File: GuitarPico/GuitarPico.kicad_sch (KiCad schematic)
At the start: 132 parts, among them J1 INPUT, J2 INPUT, J3 OUTPUT, J4 OUTPUT, J5 Barrel_Jack_Switch, J6 VGA, J8 INPUT, J9 INPUT, Q1 2N3904, Q2 2N3904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

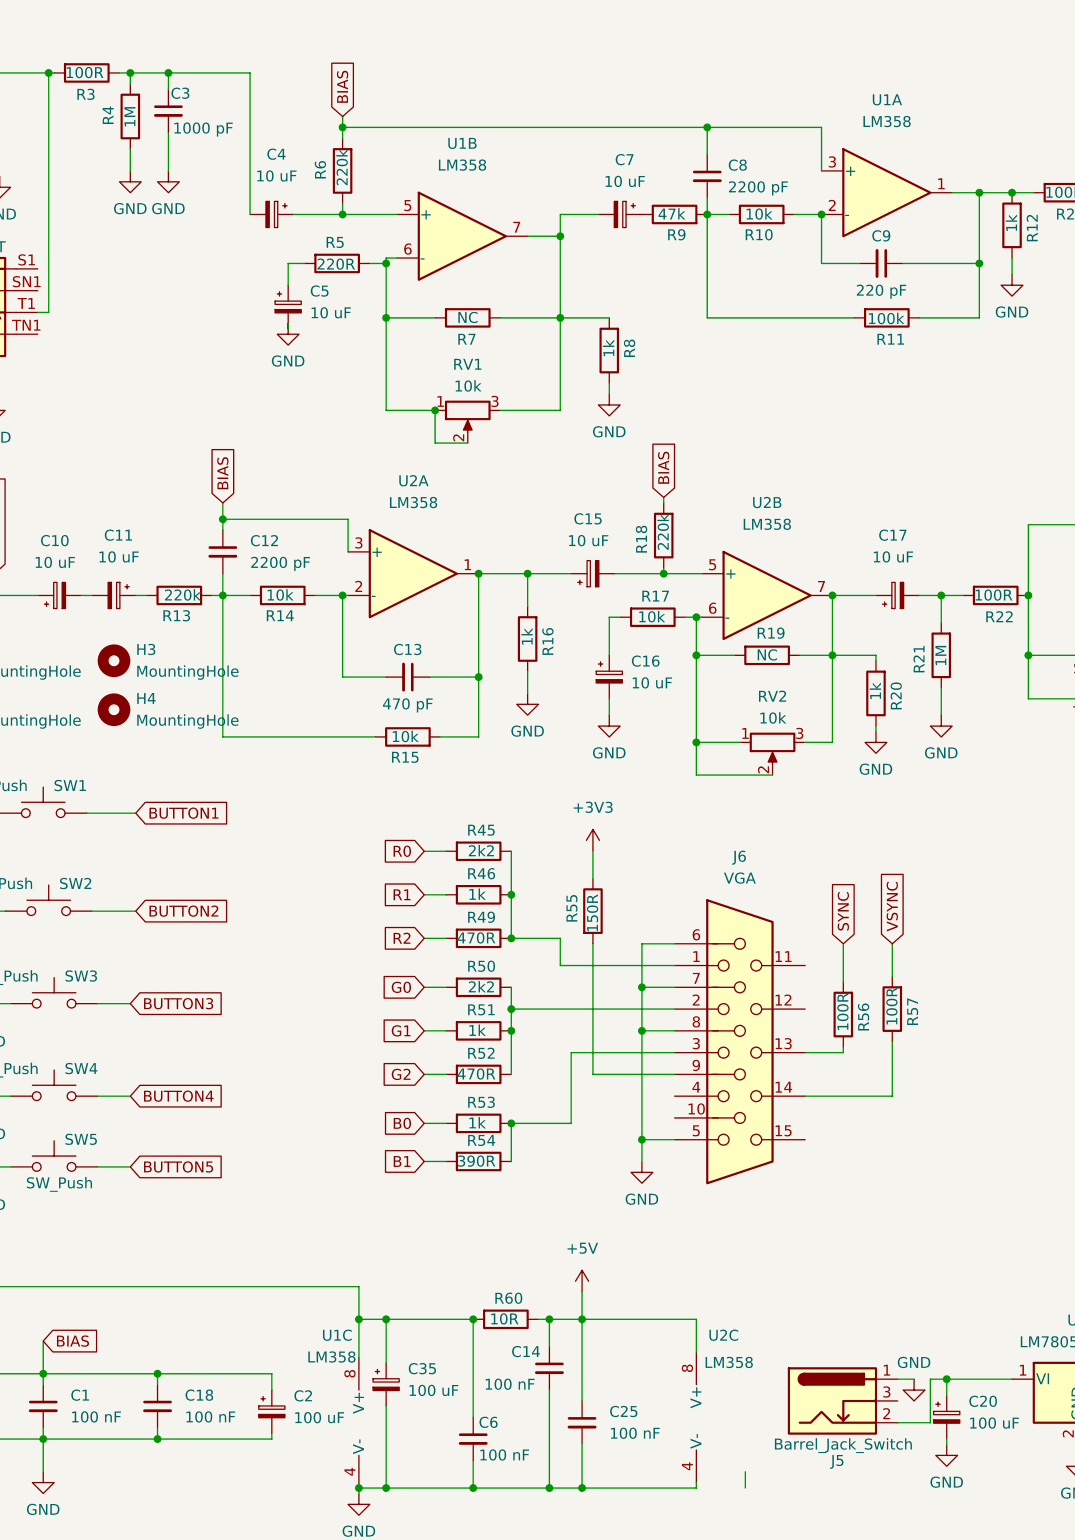
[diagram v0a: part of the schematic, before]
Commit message: Added STL file for pedal enclosure
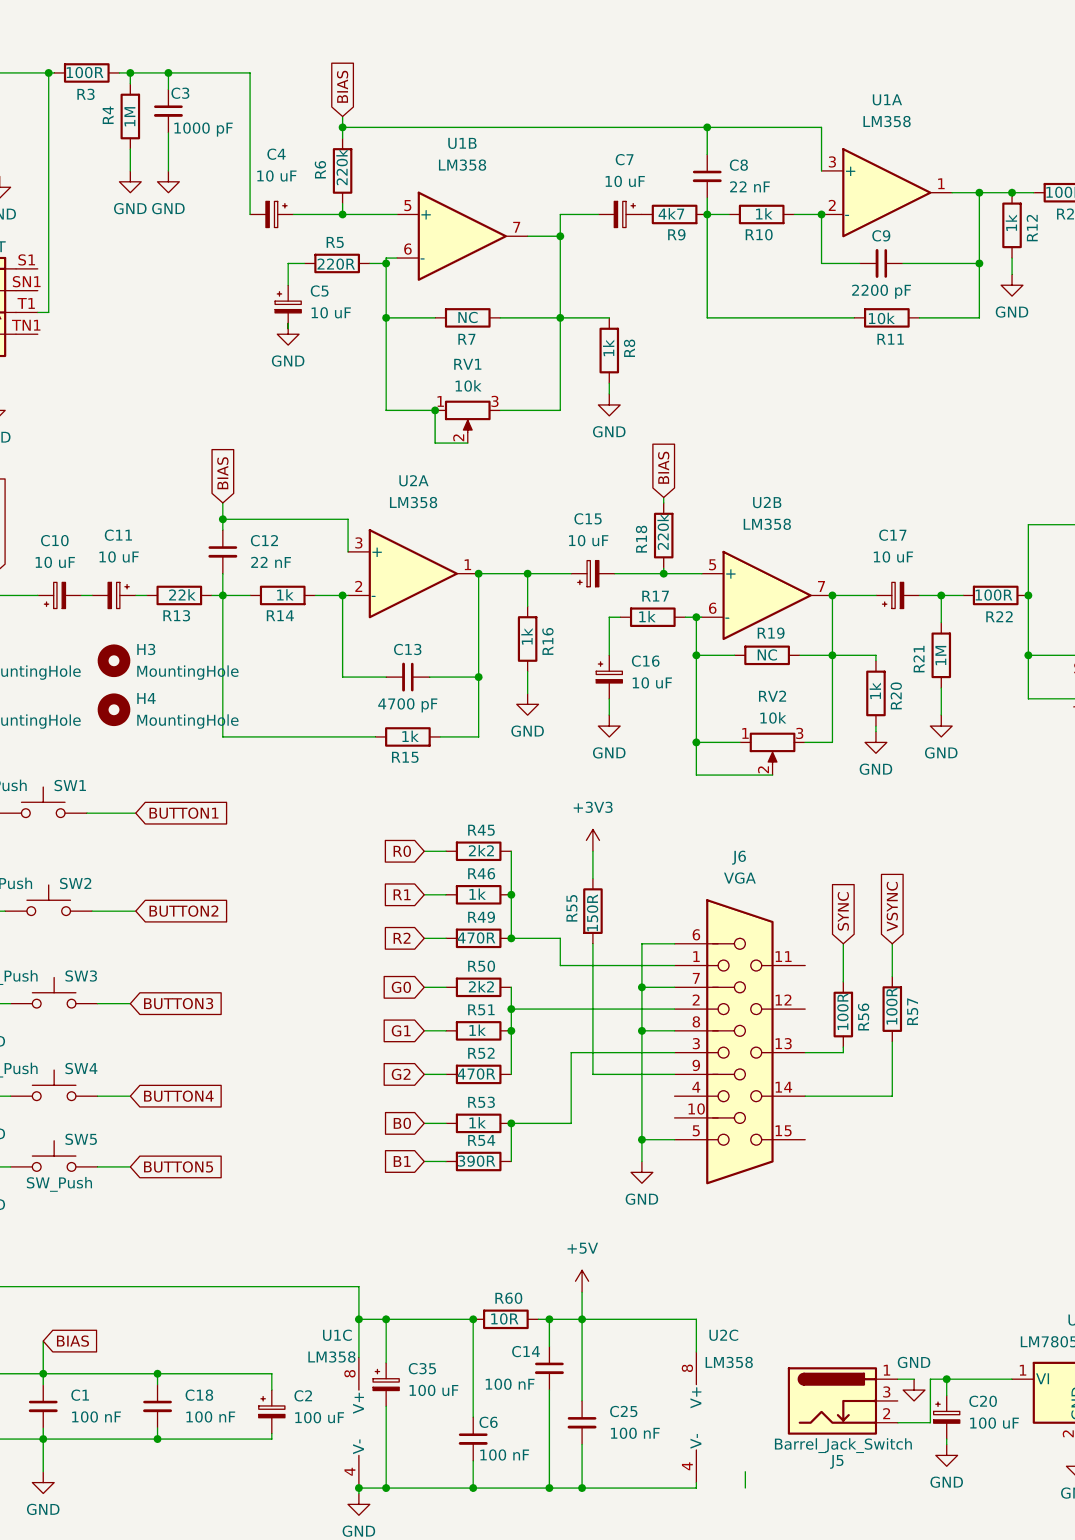
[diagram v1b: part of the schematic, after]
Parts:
- C12, C8: value 2200 pF -> 22 nF
- C13: value 470 pF -> 4700 pF
- C9: value 220 pF -> 2200 pF
- R10, R14, R15, R17: value 10k -> 1k
- R11: value 100k -> 10k
- R13: value 220k -> 22k
- R9: value 47k -> 4k7
